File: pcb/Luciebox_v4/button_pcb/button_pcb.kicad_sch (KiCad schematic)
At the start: 67 parts, among them T1 terminal_8x1, T2 terminal_8x1

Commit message: V4 main pcb ready for layouting
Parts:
- removed D1, D2, D3, D4, D5, D6, D7, D8: D_Schottky, Luciebox_components:smd_throughhole_2_pins, symbol Luciebox_components:D_Schottky
- removed H1, H10, H12, H14, H15, H17, H7, H8, H9: MountingHole, Luciebox_components:MountingHole_4.3mm_M4, symbol Luciebox_components:MountingHole
- removed R1, R10, R11, R12, R13, R14, R15, R16, R17, R18, R2, R3, R4, R5, R6, R7, R8, R9: R_Small, Luciebox_components:1206_0805, symbol Luciebox_components:R_Small
- removed R19, R20, R21, R22, R23, R24, R25, R26, R27, R28, R29, R30: 10K, Luciebox_components:1206_0805, symbol Luciebox_components:R_Small-Device
- removed S9: selector_knob, Luciebox_components:Rotary_Switch, symbol Luciebox_components:selector_knob
- added BT1: 4xAA_Battery_holder, Luciebox_components:BatteryHolder_4xAA, symbol Luciebox_components:4xAA_Battery_holder
- added T3: terminal_8x1, Luciebox_components:Terminal_8x1_100mil, symbol Luciebox_components:terminal_8x1
- added T4: terminal_2x1, Luciebox_components:Terminal_2x1_100mil, symbol Luciebox_components:terminal_2x1
- S1, S2, S3, S4, S5, S6, S7, S8: footprint Luciebox_components:button_LAZ16-11 -> Luciebox_components:button_LAZ16-11_big_holes
- renumbered H16 to H1, H6 to H2, H13 to H3, H11 to H4, H3 to H6, H2 to H7, H4 to H8
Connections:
- net ANALOG_1 is gone; now on net common Anode: T1.3
- net GND: no longer S1.2 (NC)
- net VCC: no longer S1.1 (NO), S1.5 (LED_-), S2.5 (LED_-), S3.5 (LED_-)
- net at T2.8: now also S8.5 (LED_-)
- net at S4.3 (C): now also T3.4
- net at S1.3 (C): now also T1.7
- net common Anode: now reaches S1.4 (LED_+), S2.4 (LED_+), S3.4 (LED_+), S4.4 (LED_+), S5.4 (LED_+), S6.4 (LED_+), S7.4 (LED_+), S8.4 (LED_+), connect_for_vcc_as_common_anode1.2
- net common Anode: no longer T1.6
- net at T2.4: now also S4.5 (LED_-)
- net at S8.3 (C): now also T3.8
- net at S3.3 (C): now also T3.3
- net at T2.5: now also S5.5 (LED_-)
- net at S6.3 (C): now also T3.6
- net at S2.3 (C): now also T3.2
- net at S6.5 (LED_-): now also T2.6
- net at T1.5: now also S1.1 (NO), BT1.1 (+), T4.2
- net at T2.2: now also S2.5 (LED_-)
- net at T2.1: now also S1.5 (LED_-)
- net at T2.3: now also S3.5 (LED_-)
- net at T2.7: now also S7.5 (LED_-)
- net at S7.3 (C): now also T3.7
- net at S5.3 (C): now also T3.5
- net ANALOG_2: no longer names the net of T1.4
- net ANALOG_2: now also BT1.2 (-), T4.1
- new net: S1.2 (NC), T1.6
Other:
- note added: "S1 is connected to Vbat+ for single touch power ON and autopower OFF"
- moved on the sheet: H1, H2, H3, H4, H5, H6, H7, H8

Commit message: layout main board start
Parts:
- added U1: 8X8PADS, Luciebox_components:8X8PADS_100mil, symbol Luciebox_components:8X8PADS
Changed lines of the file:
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@@
     (pin "1")
+  )
+  (symbol (lib_id "Luciebox_components:8X8PADS") (at 212.09 54.61 0) (unit 1)
+    (in_bom yes) (on_board yes) (fields_autoplaced)
+    (property "Reference" "U1" (id 0) (at 234.95 40.6399 0)
+      (effects (font (size 1.27 1.27)) (justify left))
+    )
+    (property "Value" "8X8PADS" (id 1) (at 234.95 43.1799 0)
+      (effects (font (size 1.27 1.27)) (justify left))
+    )
+    (property "Footprint" "Luciebox_components:8X8PADS_100mil" (id 2) (at 212.09 54.61 0)
+      (effects (font (size 1.27 1.27)) hide)
+    )
+    (property "Datasheet" "" (id 3) (at 212.09 54.61 0)
+      (effects (font (size 1.27 1.27)) hide)
+    )
+    (pin "1")
+    (pin "10")
+    (pin "11")
+    (pin "12")
+    (pin "13")
+    (pin "14")
+    (pin "15")
+    (pin "16")
+    (pin "17")
+    (pin "18")
+    (pin "19")
+    (pin "2")
+    (pin "20")
+    (pin "21")
+    (pin "22")
+    (pin "23")
+    (pin "24")
+    (pin "25")
+    (pin "26")
+    (pin "27")
+    (pin "28")
+    (pin "29")
+    (pin "3")
+    (pin "30")
+    (pin "31")
+    (pin "32")
+    (pin "33")
+    (pin "34")
+    (pin "35")
+    (pin "36")
+    (pin "37")
+    (pin "38")
+    (pin "39")
+    (pin "4")
+    (pin "40")
+    (pin "41")
+    (pin "42")
+    (pin "43")
+    (pin "44")
+    (pin "45")
+    (pin "46")
+    (pin "47")
+    (pin "48")
+    (pin "49")
+    (pin "5")
+    (pin "50")
+    (pin "51")
+    (pin "52")
+    (pin "53")
+    (pin "54")
+    (pin "55")
+    (pin "56")
+    (pin "57")
+    (pin "58")
+    (pin "59")
+    (pin "6")
+    (pin "60")
+    (pin "61")
+    (pin "62")
+    (pin "63")
+    (pin "64")
+    (pin "7")
+    (pin "8")
+    (pin "9")
   )
   (symbol (lib_id "power:VCC") (at 66.04 39.37 0) (unit 1)
@@
       (reference "T4") (unit 1) (value "terminal_2x1") (footprint "Luciebox_components:Terminal_2x1_100mil")
     )
+    (path "/a2a33a3d-c501-4e33-b67b-7d07ef8aa4a7"
+      (reference "U1") (unit 1) (value "8X8PADS") (footprint "Luciebox_components:8X8PADS_100mil")
+    )
     (path "/e40ae1ad-2f90-437b-a507-1eecc9638bd0"

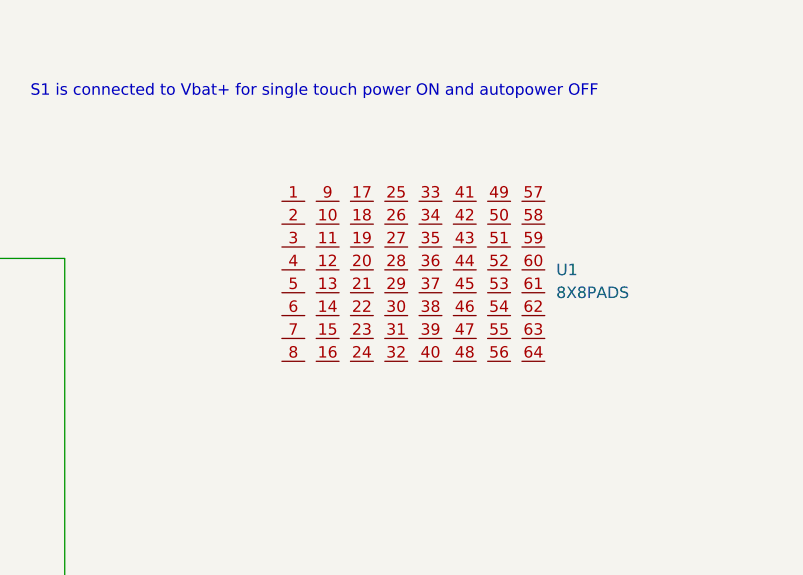
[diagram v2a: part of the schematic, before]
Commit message: Delete Arduino Uno footprint. Line up bottonboard and main pcb
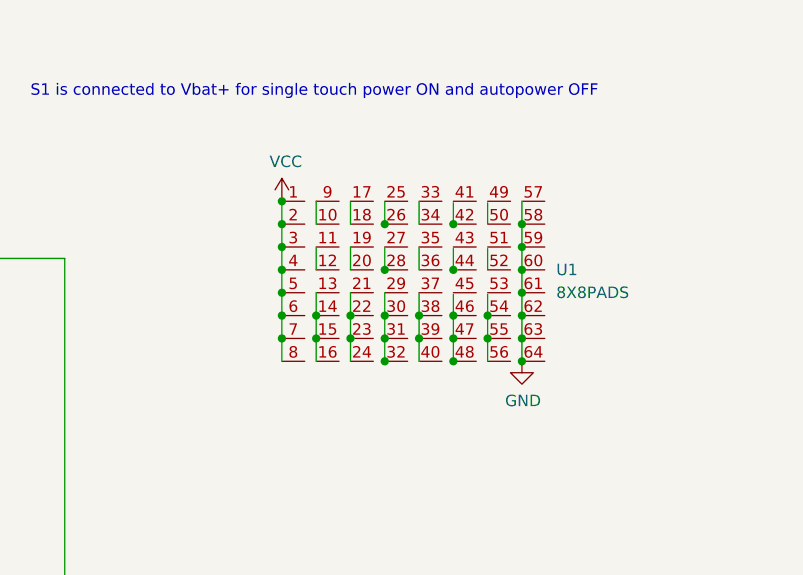
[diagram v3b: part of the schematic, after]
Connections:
- net GND: now also U1.57, U1.58, U1.59, U1.60, U1.61, U1.62, U1.63, U1.64
- net VCC: now also U1.1, U1.2, U1.3, U1.4, U1.5, U1.6, U1.7, U1.8
- net at U1.10: now also U1.9
- net at U1.11: now also U1.12
- net at U1.13: now also U1.14, U1.15, U1.16
- net at U1.17: now also U1.18
- net at U1.19: now also U1.20
- net at U1.21: now also U1.22, U1.23, U1.24
- net at U1.30: now also U1.31, U1.32
- net at U1.38: now also U1.39, U1.40
- net at U1.46: now also U1.47, U1.48
- net at U1.54: now also U1.55, U1.56
